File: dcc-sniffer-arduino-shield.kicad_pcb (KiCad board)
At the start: 2 copper layers, 1 part

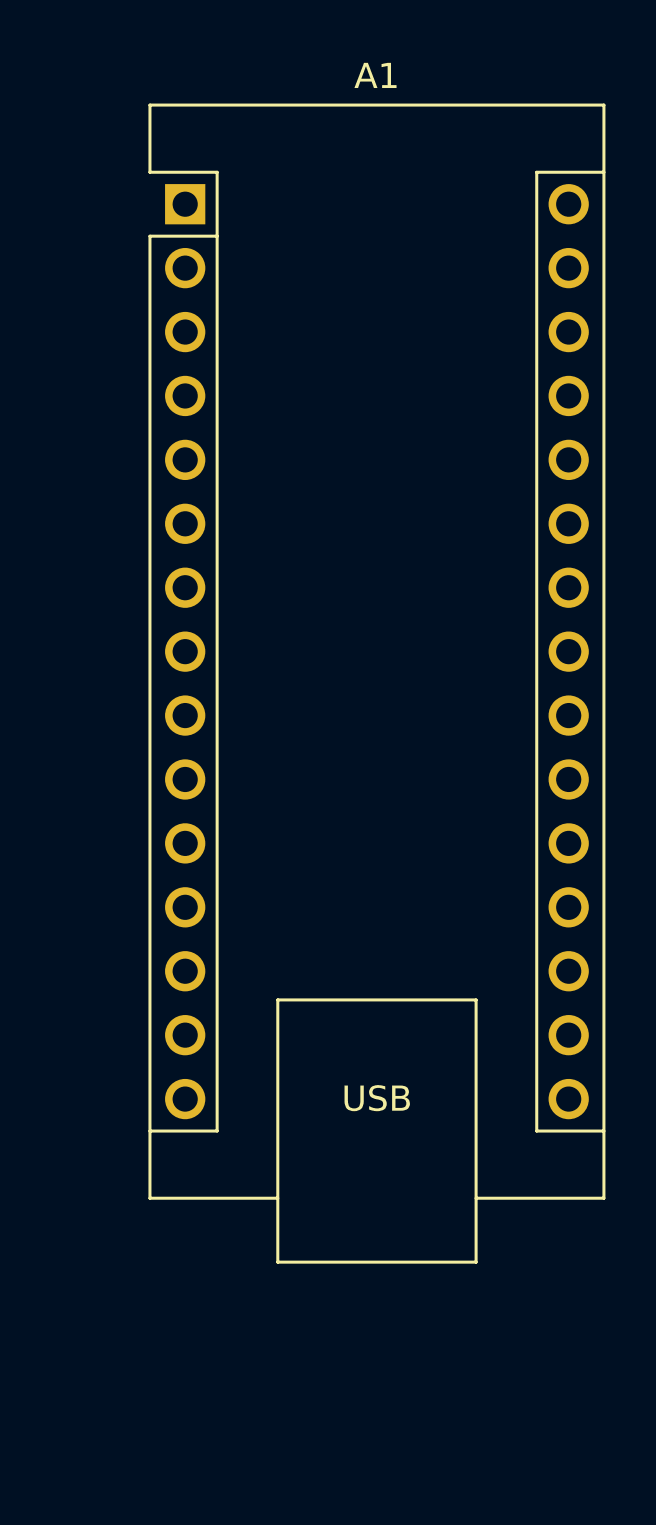
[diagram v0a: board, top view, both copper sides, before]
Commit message: Route PCB.
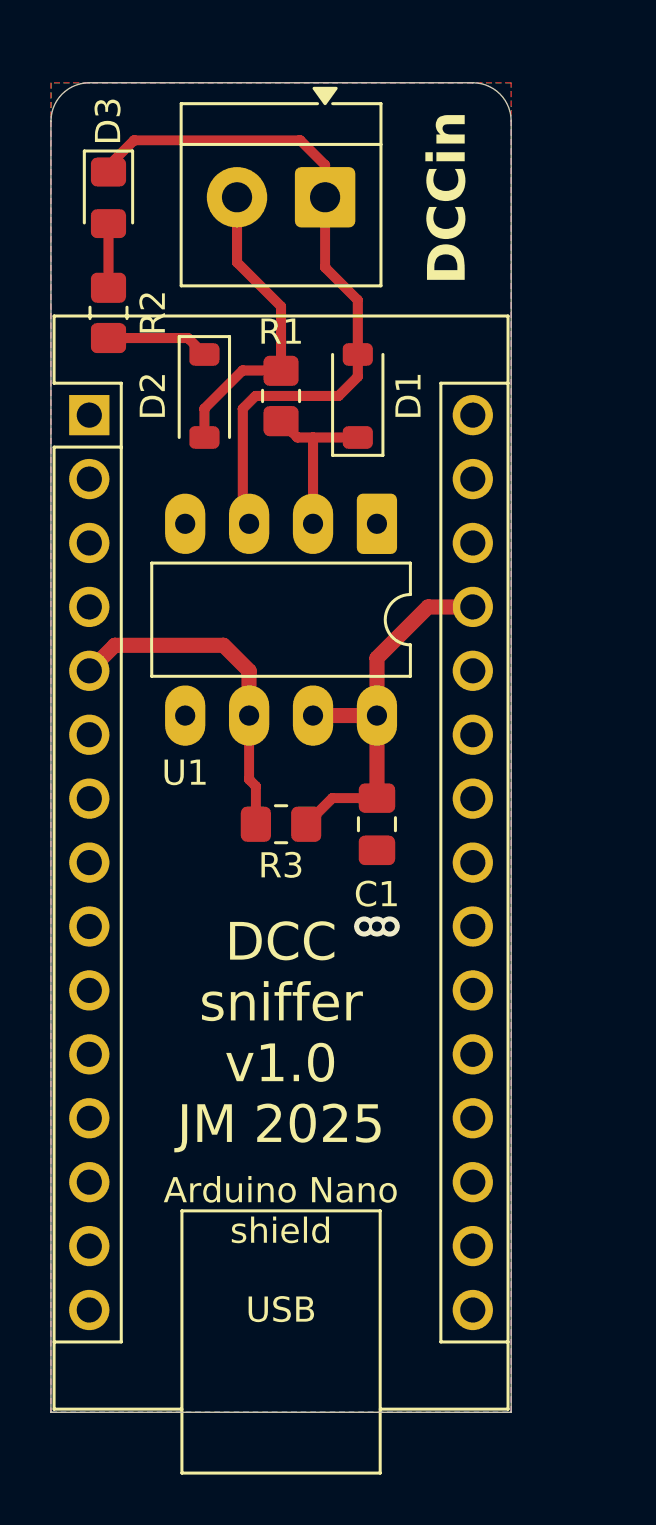
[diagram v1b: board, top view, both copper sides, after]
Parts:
- added C1: 100n, Capacitor_SMD:C_0805_2012Metric_Pad1.18x1.45mm_HandSolder, F.Cu at (165.6, 101.1)
- added D1: 1N5819, Diode_SMD:D_SOD-123, F.Cu at (164.8, 84.1)
- added D2: 1N5819, Diode_SMD:D_SOD-123, F.Cu at (158.8, 84.1)
- added D3: GREEN, LED_SMD:LED_0805_2012Metric_Pad1.15x1.40mm_HandSolder, F.Cu at (154.9, 76.2)
- added J1: MV132, TerminalBlock_4Ucon:TerminalBlock_4Ucon_1x02_P3.50mm_Horizontal, F.Cu at (163.5, 76.2)
- added R1: 1k5, Resistor_SMD:R_0805_2012Metric_Pad1.20x1.40mm_HandSolder, F.Cu at (161.8, 84.1)
- added R2: 10k, Resistor_SMD:R_0805_2012Metric_Pad1.20x1.40mm_HandSolder, F.Cu at (154.9, 80.8)
- added R3: 10k, Resistor_SMD:R_0805_2012Metric_Pad1.20x1.40mm_HandSolder, F.Cu at (161.8, 101.1)
- added U1: 6N137, Package_DIP:DIP-8_W7.62mm_LongPads, F.Cu at (165.6, 89.2)
- moved A1 9.21 mm to (154.2, 84.8)
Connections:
- net Net-(A1-GND-Pad29) renamed GND
- A1 pad 27: unconnected-(A1-+5V-Pad27) -> +5V
- A1 pad 5: unconnected-(A1-D2-Pad5) -> Net-(A1-D2)
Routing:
- net /K: track 0.00 -> 28.4 mm
- net +5V: track 0.00 -> 16.0 mm
- net Net-(A1-D2): track 0.00 -> 13.4 mm
- net /J: track 0.00 -> 12.4 mm
- net Net-(D1-K): track 0.00 -> 6.75 mm
- net Net-(D2-K): track 0.00 -> 4.08 mm
- net Net-(D3-A): track 0.00 -> 2.55 mm
- net GND: vias 0 -> 3
- added copper zone on B.Cu, net GND
- added copper zone on F.Cu, net GND
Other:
- board outline added: 18.3 x 52.8 mm
- board text added: "Arduino Nano shield"
- board text added: "DCC sniffer v1.0 JM 2025"
- board text added: "DCCin"
